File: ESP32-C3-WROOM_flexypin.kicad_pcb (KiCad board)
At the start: 2 copper layers, 31 x 28.6 mm, 14 parts, among them J1 Conn_01x09, J19 USB_C_Receptacle_USB2.0_14P, J2 Conn_01x09, J22 Conn_01x09, J3 Conn_01x09, SW1 SW_Push, SW3 SW_Push, U1 RT9080

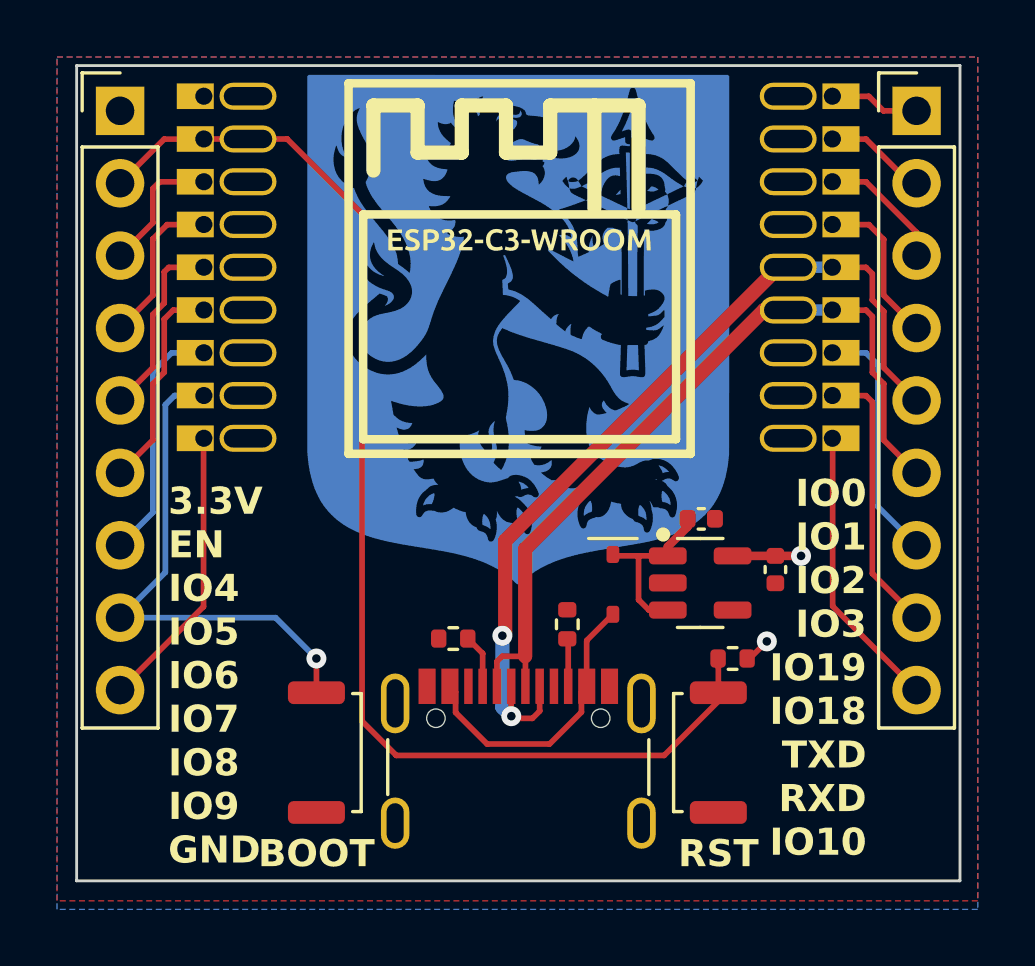
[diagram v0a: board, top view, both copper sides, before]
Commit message: added LED
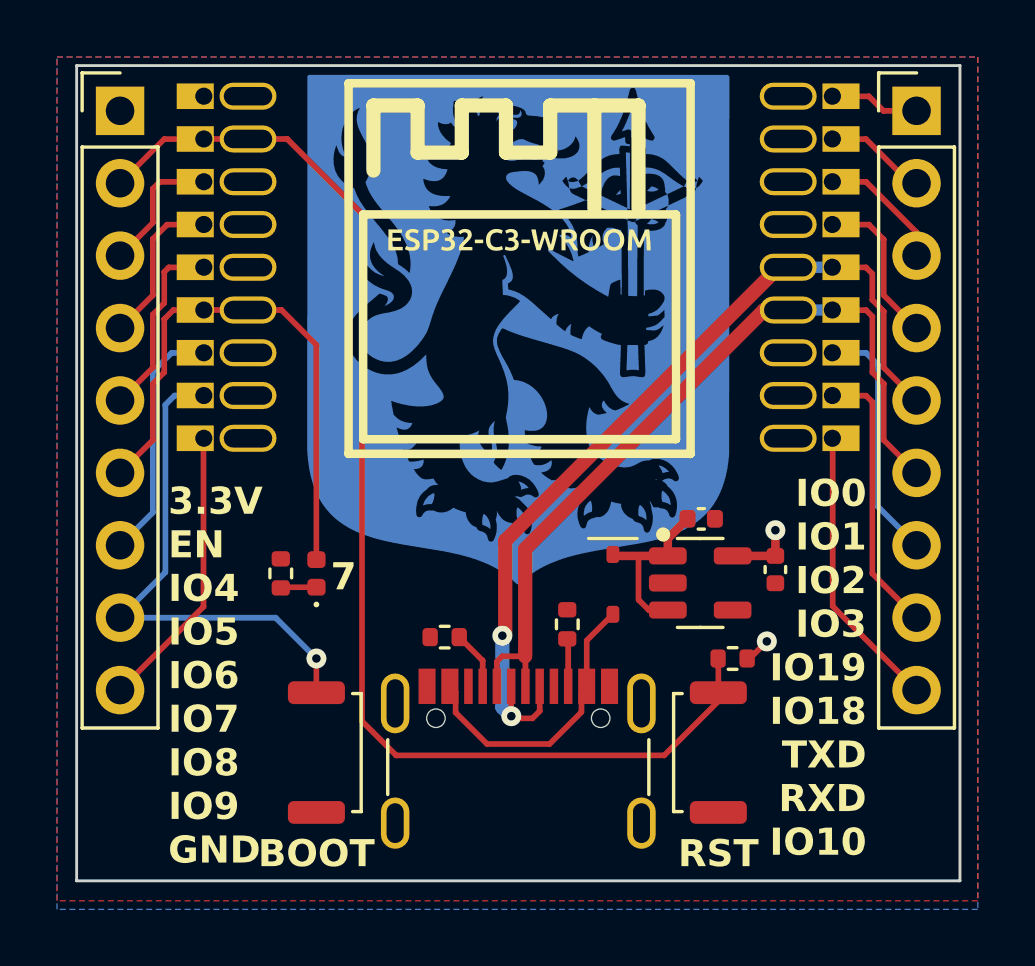
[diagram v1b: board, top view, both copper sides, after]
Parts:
- added D2: LED_Small, LED_SMD:LED_0402_1005Metric, F.Cu at (141.0, 98.0)
- added R4: 100-1kΩ, Resistor_SMD:R_0402_1005Metric, F.Cu at (139.8, 98.0)
- moved R2 0.30 mm to (145.5, 100.2)
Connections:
- net /IO7 renamed IO7
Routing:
- net IO7: track 7.54 -> 19.5 mm
- net Net-(D2-K): track 0.00 -> 1.26 mm
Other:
- board text added: "7"
